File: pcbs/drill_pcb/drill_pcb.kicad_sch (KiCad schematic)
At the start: 92 parts, among them J10 TOF_senzor, J11 Screw_Terminal_01x03, J12 Screw_Terminal_01x03, J2 Screw_Terminal_01x06, J4 motor1, J5 Screw_Terminal_01x03, J6 Screw_Terminal_01x03, J7 Screw_Terminal_01x06, J8 motor2, SW1 RPi reset, SW2 SW_Push, SW3 SW_Push, SW4 SW_Push, U1 PCA9306, U2 Pico, U4 IFX007T, U5 IFX007T, U6 ACS712xLCTR-20A, U7 HT75xx-1-SOT89

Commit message: zasobnik ready na 24V
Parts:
- removed A2: Arduino_Nano_v3.x, Module:Arduino_Nano, symbol drill_arduinoNanoEdit:arduinoNanoEdit
- removed A7: ~, drill_hx711footp:HX711, symbol HX711:HX711A
- removed C14, C15: 10n, Capacitor_THT:C_Disc_D4.7mm_W2.5mm_P5.00mm, symbol Device:C
- removed C16, C17: C_Polarized, Capacitor_THT:CP_Radial_D5.0mm_P2.50mm, symbol Device:C_Polarized
- removed D8: TVS 12V, Diode_THT:D_DO-41_SOD81_P10.16mm_Horizontal, symbol Diode:1N4007
- removed Motor1, hall_senzor1: Screw_Terminal_01x04, TerminalBlock_TE-Connectivity:TerminalBlock_TE_282834-4_1x04_P2.54mm_Horizontal, symbol Connector:Screw_Terminal_01x04
- removed TP12, TP15, TP16: TestPoint, TestPoint:TestPoint_Pad_1.5x1.5mm, symbol Connector:TestPoint
- removed TP13: TestPoint_2Pole, Resistor_THT:R_Axial_DIN0309_L9.0mm_D3.2mm_P12.70mm_Horizontal, symbol Connector:TestPoint_2Pole
- removed TP14: TestPoint_2Pole, Capacitor_SMD:C_0504_1310Metric_Pad0.83x1.28mm_HandSolder, symbol Connector:TestPoint_2Pole
- removed Tenzometry1: Screw_Terminal_01x06, TerminalBlock_TE-Connectivity:TerminalBlock_TE_282834-6_1x06_P2.54mm_Horizontal, symbol Connector:Screw_Terminal_01x06
- removed U7: HT75xx-1-SOT89, Package_TO_SOT_THT:TO-92L_Inline, symbol Regulator_Linear:HT75xx-1-SOT89
- added 111: ~, hx711footp:HX711, symbol HX711:HX711A
- added A2: Arduino_Nano_v3.x, Module:Arduino_Nano, symbol MCU_Module:Arduino_Nano_v3.x
- added C1, C2: 10n, Capacitor_THT:C_Disc_D4.7mm_W2.5mm_P5.00mm, symbol Device:C
- added C14, C15: C_Polarized, Capacitor_THT:CP_Radial_D5.0mm_P2.50mm, symbol Device:C_Polarized
- added J14: Screw_Terminal_01x06, TerminalBlock_TE-Connectivity:TerminalBlock_TE_282834-6_1x06_P2.54mm_Horizontal, symbol Connector:Screw_Terminal_01x06
- added J15, J3: Screw_Terminal_01x04, TerminalBlock_TE-Connectivity:TerminalBlock_TE_282834-4_1x04_P2.54mm_Horizontal, symbol Connector:Screw_Terminal_01x04
- added U3: HT75xx-1-SOT89, Package_TO_SOT_THT:TO-92L_Inline, symbol Regulator_Linear:HT75xx-1-SOT89
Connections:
- net +12V is gone; now on net +24V: D9.2 (A)
- net +5V: now also A3.13 (~{RESET}), A3.2 (VDD), R14.2, TP10.1, TP11.1, TP4.1, TP9.1, 111.VCC, A2.27 (+5V)
- net GND: now also TP5.1, 111.GND, A2.29 (GND), A2.4 (GND), C1.1, C14.2, C15.2, C2.1, J15.3 (Pin_3), U3.1 (GND); no longer TP4.1
- net SCL: now also A2.24 (A5)
- net SDA: now also A2.23 (A4)
- net +23,3V: now reaches D9.1 (K)
- net +23,3V: now also A3.8 (VMOT), C14.1, U3.2 (VIN)
- net BTN_GRN: now reaches C13.2
- net BTN_GRN: now also R13.1, A2.7 (D4); no longer R11.1
- net at TP8.1: now also A2.22 (A3)
- net BTN_RED: now reaches R12.1
- net BTN_RED: now also A2.12 (D9), C2.2
- net at TP1.1: now also A2.14 (D11)
- net at TP2.1: now also A2.15 (D12)
- net at TP7.1: now also A2.21 (A2)
- net at A3.3 (1B): now also J3.1 (Pin_1)
- net at A3.4 (1A): now also J3.2 (Pin_2)
- net at A3.5 (2A): now also J3.3 (Pin_3)
- net at A3.6 (2B): now also J3.4 (Pin_4)
- net DRIV_SLP: now reaches A3.14 (~{SLEEP})
- net DRIV_SLP: now also A2.9 (D6)
- net DRIV_STP: now reaches A3.15 (STEP)
- net DRIV_STP: now also A2.8 (D5)
- net DRIV_DIR: now reaches A3.16 (DIR)
- net DRIV_DIR: now also A2.6 (D3)
- net at TP6.1: now also A2.20 (A1)
- new net: C15.1, J15.1 (Pin_1), J15.4 (Pin_4), U3.3 (VOUT)
- new net: A2.17 (3V3), TP3.1
- new net: 111.E+, J14.1 (Pin_1)
- new net: 111.E-, J14.2 (Pin_2)
- new net: 111.A-, J14.3 (Pin_3)
- new net: 111.A+, J14.4 (Pin_4)
- new net: 111.B-, J14.5 (Pin_5)
- new net: 111.B+, J14.6 (Pin_6)
- new net ADC_DT: 111.DT, A2.10 (D7)
- new net ADC_SCK: 111.SCK, A2.11 (D8)
- new net BTN_YEL: A2.13 (D10), C1.2, R11.1
- new net HALL_SIG: A2.19 (A0), J15.2 (Pin_2)
- now unconnected: A3.9 (~{ENABLE})
- no-connect marks 85 -> 87
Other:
- note added: "Zapojeni driveru"
- note added: "Zapojeni enkoderu"
- note added: "Zapojeni mikrokontroleru"
- note added: "Zapojeni napajeni"
- note added: "Zapojeni ovladacich tlacitek"
- note added: "Zapojeni prevodniku"
- moved on the sheet: A1, A4, A5, A6, C10, C11, C12, C22, C23, C3, C4, C5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

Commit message: Schematic divided into subsheets
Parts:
- removed 111: ~, hx711footp:HX711, symbol HX711:HX711A
- removed A1, A4: Arduino_Nano_v3.x, Module:Arduino_Nano, symbol drill_arduinoNanoEdit:arduinoNanoEdit
- removed A2: Arduino_Nano_v3.x, Module:Arduino_Nano, symbol MCU_Module:Arduino_Nano_v3.x
- removed A3: Pololu_Breakout_A4988, Module:Pololu_Breakout-16_15.2x20.3mm, symbol Driver_Motor:Pololu_Breakout_A4988
- removed A5, A6: Driver_TMC2209, Module:Pololu_Breakout-16_15.2x20.3mm, symbol mujDriver:mujDriver2
- removed C1, C13, C2: 10n, Capacitor_THT:C_Disc_D4.7mm_W2.5mm_P5.00mm, symbol Device:C
- removed C10, C3, C4, C5: 100n, Capacitor_SMD:C_1206_3216Metric_Pad1.33x1.80mm_HandSolder, symbol Device:C
- removed C11, C6, C9: 1n, Capacitor_SMD:C_1206_3216Metric_Pad1.33x1.80mm_HandSolder, symbol Device:C
- removed C12: 1000uF/50V, Capacitor_THT:CP_Radial_D12.5mm_P5.00mm, symbol Device:C_Polarized
- removed C14, C15: C_Polarized, Capacitor_THT:CP_Radial_D5.0mm_P2.50mm, symbol Device:C_Polarized
- removed C22, C23: 100μ, Capacitor_THT:CP_Radial_D8.0mm_P3.50mm, symbol Device:C_Polarized
- removed C7, C8: 100n/50V, Capacitor_SMD:C_1206_3216Metric_Pad1.33x1.80mm_HandSolder, symbol Device:C
- removed D3, D4: SMAJ5.0CA, Diode_SMD:D_SMA, symbol Diode:SMAJ5.0CA
- removed D5, D6, D7: SFH4550, LED_THT:LED_D5.0mm_IRGrey, symbol LED:SFH4550
- removed D9: 1N4007, Diode_THT:D_DO-41_SOD81_P10.16mm_Horizontal, symbol Diode:1N4007
- removed Dean2: Motor, drill_T-DEAN:DEANS, symbol Connector:Screw_Terminal_01x02
- removed J10: TOF_senzor, Connector_JST:JST_XH_B3B-XH-A_1x03_P2.50mm_Vertical, symbol Connector:Screw_Terminal_01x03
- removed J11, J12, J5, J6: Screw_Terminal_01x03, Connector_JST:JST_XH_S3B-XH-A-1_1x03_P2.50mm_Horizontal, symbol Connector:Screw_Terminal_01x03
- removed J14: Screw_Terminal_01x06, TerminalBlock_TE-Connectivity:TerminalBlock_TE_282834-6_1x06_P2.54mm_Horizontal, symbol Connector:Screw_Terminal_01x06
- removed J15, J3: Screw_Terminal_01x04, TerminalBlock_TE-Connectivity:TerminalBlock_TE_282834-4_1x04_P2.54mm_Horizontal, symbol Connector:Screw_Terminal_01x04
- removed J2: Screw_Terminal_01x06, Connector_JST:JST_XH_B6B-XH-A_1x06_P2.50mm_Vertical, symbol Connector:Screw_Terminal_01x06
- removed J4: motor1, Connector_JST:JST_XH_B4B-XH-A_1x04_P2.50mm_Vertical, symbol Connector:Screw_Terminal_01x04
- removed J7: Screw_Terminal_01x06, Connector_JST:JST_XH_S6B-XH-A-1_1x06_P2.50mm_Horizontal, symbol Connector:Screw_Terminal_01x06
- removed J8: motor2, Connector_JST:JST_XH_B4B-XH-A_1x04_P2.50mm_Vertical, symbol Connector:Screw_Terminal_01x04
- removed JST1: Thermometer, Connector_JST:JST_XH_B3B-XH-A_1x03_P2.50mm_Vertical, symbol Connector:Screw_Terminal_01x03
- removed R1: 4k7, Resistor_SMD:R_1206_3216Metric_Pad1.30x1.75mm_HandSolder, symbol Device:R
- removed R10: 330k, Resistor_SMD:R_1206_3216Metric_Pad1.30x1.75mm_HandSolder, symbol Device:R
- removed R11, R12, R13, R14: 10k, Resistor_THT:R_Axial_DIN0207_L6.3mm_D2.5mm_P10.16mm_Horizontal, symbol Device:R
- removed R15: 1k, Resistor_SMD:R_1206_3216Metric, symbol Device:R
- removed R2, R3, R4, R5, R6, R7: 10k, Resistor_SMD:R_1206_3216Metric_Pad1.30x1.75mm_HandSolder, symbol Device:R
- removed R8, R9: 820, Resistor_SMD:R_1206_3216Metric_Pad1.30x1.75mm_HandSolder, symbol Device:R
- removed SW2, SW3, SW4: SW_Push, Button_Switch_THT:SW_PUSH_6mm, symbol Switch:SW_Push
- removed TP1, TP2, TP3, TP4, TP5, TP6, TP7, TP8: TestPoint, TestPoint:TestPoint_Pad_1.5x1.5mm, symbol Connector:TestPoint
- removed TP10, TP11, TP9: TestPoint_2Pole, Capacitor_SMD:C_0504_1310Metric_Pad0.83x1.28mm_HandSolder, symbol Connector:TestPoint_2Pole
- removed U3: HT75xx-1-SOT89, Package_TO_SOT_THT:TO-92L_Inline, symbol Regulator_Linear:HT75xx-1-SOT89
- removed U4, U5: IFX007T, drill_IFX007T:TO127P1500X440-8N_plusVias, symbol drill_IFX007T:IFX007T_uprava
- removed U6: ACS712xLCTR-20A, Package_SO:SOIC-8_3.9x4.9mm_P1.27mm, symbol Sensor_Current:ACS712xLCTR-20A
- renumbered D1 to D101, D2 to D102, Dean1 to Dean101, F1 to F101, F2 to F102, SW1 to SW101, U1 to U101, U2 to U102, V1 to V101
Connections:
- net SCL renamed Linear drive control/SCL
- net SDA renamed Linear drive control/SDA
- no-connect marks 87 -> 38
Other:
- added sheet Linear drive control (linearDriveControl.kicad_sch)
- added sheet Motor control (motorControl.kicad_sch)
- added sheet Storage and weighing (storageAndWeighing.kicad_sch)
- note removed: "Linear motors control"
- note removed: "Motor control"
- note removed: "Storage and weighing"
- note removed: "Zapojeni driveru"
- note removed: "Zapojeni enkoderu"
- note removed: "Zapojeni mikrokontroleru"
- note removed: "Zapojeni napajeni"
- note removed: "Zapojeni ovladacich tlacitek"
- note removed: "Zapojeni prevodniku"
- moved on the sheet: D102, SW101, U101, U102

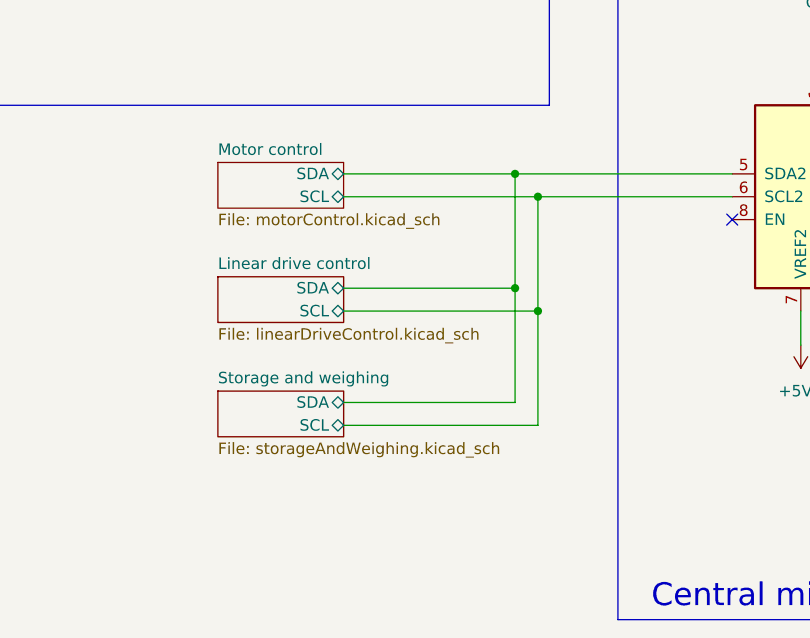
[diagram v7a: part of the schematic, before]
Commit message: added RESET connections into subsheets
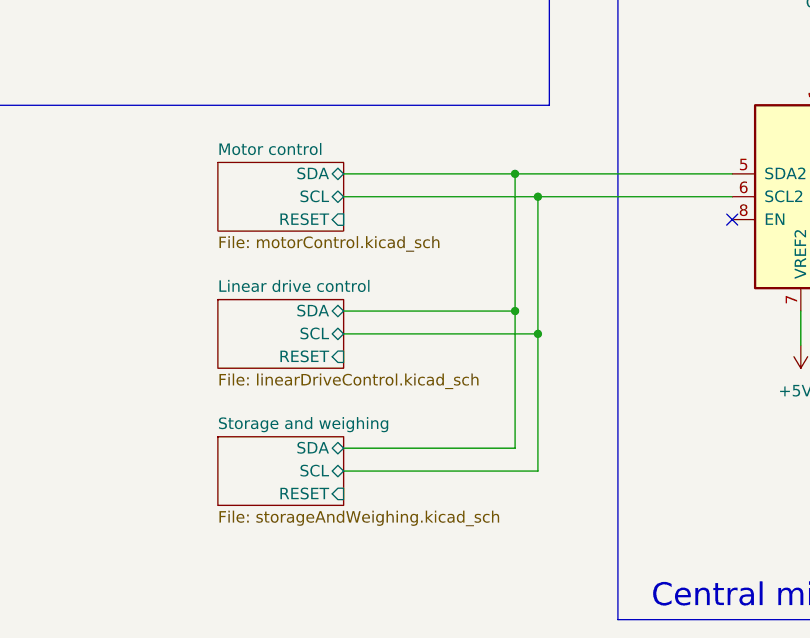
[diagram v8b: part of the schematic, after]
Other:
- sheet Linear drive control ports: added RESET; removed none
- sheet Motor control ports: added RESET; removed none
- sheet Storage and weighing ports: added RESET; removed none
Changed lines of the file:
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@@
 	)
 	(junction
-		(at 133.35 74.93)
+		(at 135.89 80.01)
 		(diameter 0)
 		(color 0 0 0 0)
 	)
 	(junction
-		(at 135.89 77.47)
+		(at 133.35 77.47)
 		(diameter 0)
 		(color 0 0 0 0)
@@
 	(wire
 		(pts
-			(xy 133.35 62.23) (xy 133.35 74.93)
+			(xy 135.89 80.01) (xy 135.89 95.25)
 		)
 		(stroke
@@
 	(wire
 		(pts
-			(xy 135.89 64.77) (xy 135.89 77.47)
-		)
-		(stroke
-			(width 0)
-			(type default)
-		)
-	)
-	(wire
-		(pts
 			(xy 91.44 34.29) (xy 92.71 34.29)
 		)
@@
 	(wire
 		(pts
-			(xy 114.3 74.93) (xy 133.35 74.93)
+			(xy 114.3 77.47) (xy 133.35 77.47)
 		)
 		(stroke
@@
 	(wire
 		(pts
-			(xy 133.35 74.93) (xy 133.35 87.63)
+			(xy 133.35 62.23) (xy 133.35 77.47)
 		)
 		(stroke
@@
 	(wire
 		(pts
-			(xy 114.3 87.63) (xy 133.35 87.63)
-		)
-		(stroke
-			(width 0)
-			(type default)
-		)
-	)
-	(wire
-		(pts
-			(xy 114.3 77.47) (xy 135.89 77.47)
+			(xy 114.3 92.71) (xy 133.35 92.71)
+		)
+		(stroke
+			(width 0)
+			(type default)
+		)
+	)
+	(wire
+		(pts
+			(xy 114.3 80.01) (xy 135.89 80.01)
 		)
 		(stroke
@@
 	(wire
 		(pts
-			(xy 135.89 77.47) (xy 135.89 90.17)
+			(xy 135.89 64.77) (xy 135.89 80.01)
 		)
 		(stroke
@@
 	(wire
 		(pts
-			(xy 114.3 90.17) (xy 135.89 90.17)
+			(xy 133.35 77.47) (xy 133.35 92.71)
+		)
+		(stroke
+			(width 0)
+			(type default)
+		)
+	)
+	(wire
+		(pts
+			(xy 114.3 95.25) (xy 135.89 95.25)
 		)
 		(stroke
@@
 	(sheet
 		(at 100.33 60.96)
-		(size 13.97 5.08)
+		(size 13.97 7.62)
 		(fields_autoplaced yes)
 		(stroke
@@
 		)
 		(property "Sheetfile" "motorControl.kicad_sch"
-			(at 100.33 66.5984 0)
+			(at 100.33 69.1384 0)
 			(effects
 				(font
@@
 			)
 		)
+		(pin "RESET" input
+			(at 114.3 67.31 0)
+			(effects
+				(font
+					(size 1.27 1.27)
+				)
+				(justify right)
+			)
+		)
 		(instances
 			(project "drill_pcb"
@@
 	)
 	(sheet
-		(at 100.33 73.66)
-		(size 13.97 5.08)
+		(at 100.33 76.2)
+		(size 13.97 7.62)
 		(fields_autoplaced yes)
 		(stroke
@@
 		)
 		(property "Sheetname" "Linear drive control"
-			(at 100.33 72.9484 0)
+			(at 100.33 75.4884 0)
 			(effects
 				(font
@@
 		)
 		(property "Sheetfile" "linearDriveControl.kicad_sch"
-			(at 100.33 79.3246 0)
+			(at 100.33 84.4046 0)
 			(effects
 				(font
@@
 		)
 		(pin "SDA" bidirectional
-			(at 114.3 74.93 0)
+			(at 114.3 77.47 0)
 			(effects
 				(font
@@
 		)
 		(pin "SCL" bidirectional
-			(at 114.3 77.47 0)
+			(at 114.3 80.01 0)
 			(effects
 				(font
@@
 			)
 		)
+		(pin "RESET" input
+			(at 114.3 82.55 0)
+			(effects
+				(font
+					(size 1.27 1.27)
+				)
+				(justify right)
+			)
+		)
 		(instances
 			(project "drill_pcb"
@@
 	)
 	(sheet
-		(at 100.33 86.36)
-		(size 13.97 5.08)
+		(at 100.33 91.44)
+		(size 13.97 7.62)
 		(fields_autoplaced yes)
 		(stroke
@@
 		)
 		(property "Sheetname" "Storage and weighing"
-			(at 100.33 85.6484 0)
+			(at 100.33 90.7284 0)
 			(effects
 				(font
@@
 		)
 		(property "Sheetfile" "storageAndWeighing.kicad_sch"
-			(at 100.33 92.0246 0)
+			(at 100.33 99.6446 0)
 			(effects
 				(font
@@
 		)
 		(pin "SDA" bidirectional
-			(at 114.3 87.63 0)
+			(at 114.3 92.71 0)
 			(effects
 				(font
@@
 		)
 		(pin "SCL" bidirectional
-			(at 114.3 90.17 0)
-			(effects
-				(font
+			(at 114.3 95.25 0)
+			(effects
+				(font
+					(size 1.27 1.27)
+				)
+				(justify right)
+			)
+		)
+		(pin "RESET" input
+			(at 114.3 97.79 0)
+			(effects
+				(font
